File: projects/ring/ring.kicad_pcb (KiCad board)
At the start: 4 copper layers, 10 x 18 mm, 4 parts, among them U1 STM32WB55CEU6TR, Y1 NX1612SA-32.000MHZ-CHP-CIS-3

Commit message: layout and schem changes
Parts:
- removed E1: NN02-101, step-footprints:XCVR_NN02-101
- added C1: C_100nF, Capacitor_SMD:C_0402_1005Metric, F.Cu at (91.0, 39.6)
- added C10: C_100nF, Capacitor_SMD:C_0402_1005Metric, F.Cu at (87.8, 26.6)
- added C11: C_100nF, Capacitor_SMD:C_0402_1005Metric, F.Cu at (90.7, 26.6)
- added C2: C_100nF, Capacitor_SMD:C_0402_1005Metric, F.Cu at (91.0, 41.6)
- added C5: C_100nF, Capacitor_SMD:C_0402_1005Metric, F.Cu at (93.8, 39.6)
- added C6: C_100nF, Capacitor_SMD:C_0402_1005Metric, F.Cu at (93.8, 41.6)
- added C7: C_4.7uF, Capacitor_SMD:C_01005_0402Metric, F.Cu at (96.4, 41.5)
- added C8: C_100nF, Capacitor_SMD:C_0402_1005Metric, F.Cu at (96.7, 39.6)
- added C9: C_4.7uF, Capacitor_SMD:C_01005_0402Metric, F.Cu at (96.4, 43.1)
- added L1: L_10uH_LQM21FN100M70L, Inductor_SMD:L_0805_2012Metric, F.Cu at (87.1, 32.6)
- added L2: L_10nH_LQG15WZ10NJ02D, Inductor_SMD:L_0402_1005Metric, F.Cu at (84.4, 35.5)
- added TP1: Test_Point_SMD, footprints:Test_Point_SMD, F.Cu at (84.0, 39.5)
- added TP2: Test_Point_SMD, footprints:Test_Point_SMD, F.Cu at (84.0, 43.5)
- added TP3: Test_Point_SMD, footprints:Test_Point_SMD, F.Cu at (89.5, 39.5)
- added TP4: Test_Point_SMD, footprints:Test_Point_SMD, F.Cu at (89.5, 43.5)
- added TP5: Test_Point_SMD, footprints:Test_Point_SMD, F.Cu at (95.0, 39.5)
- added U2: LSM6DSO32TR, step-footprints:LSM6DSO32TR, F.Cu at (75.6, 35.8)
- added U3: ANT016008LCS2442MA2, step-footprints:ANT016008LCS2442MA2, F.Cu at (69.8, 20.4)
- added U4: BQ297xy, Package_SON:WSON-6_1.5x1.5mm_P0.5mm, F.Cu at (93.9, 43.0)
- moved Y1 10.2 mm to (78.5, 30.9), turned to 0 degrees
- moved AE1 4.03 mm to (72.2, 23.8)
- moved U1 4.03 mm to (73.2, 29.1)
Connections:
- U1 pad 1: Net-(U1-Pad1) -> Net-(C1-Pad1)
- U1 pad 13: Net-(U1-Pad13) -> /CS
- U1 pad 14: Net-(U1-Pad14) -> /SCK
- U1 pad 15: Net-(U1-Pad15) -> /MISO
- U1 pad 16: Net-(U1-Pad16) -> /MOSI
- U1 pad 20: Net-(U1-Pad20) -> Net-(C1-Pad1)
- U1 pad 22: Net-(U1-Pad22) -> GND
- U1 pad 28: Net-(U1-Pad28) -> /LSM_INT1
- U1 pad 29: Net-(U1-Pad29) -> /LSM_INT2
- U1 pad 32: Net-(U1-Pad32) -> GND
- U1 pad 35: Net-(U1-Pad20) -> Net-(C1-Pad1)
- U1 pad 39: Net-(U1-Pad39) -> /SWDIO
- U1 pad 4: Net-(U1-Pad4) -> /BOOT0
- U1 pad 40: Net-(U1-Pad40) -> Net-(C1-Pad1)
- U1 pad 41: Net-(U1-Pad41) -> /SWCLK
- U1 pad 48: Net-(U1-Pad20) -> Net-(C1-Pad1)
- U1 pad 49: Net-(U1-Pad49) -> GND
- U1 pad 8: Net-(U1-Pad8) -> Net-(C1-Pad1)
- Y1 pad 1: Net-(U1-Pad25) -> Net-(U1-Pad2)
- Y1 pad 3: Net-(U1-Pad24) -> Net-(U1-Pad3)
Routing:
- net Net-(AE1-Pad1): track 1.71 -> 1.06 mm
- added copper zone on F.Cu, net /rad_plane
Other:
- outline, holes or cut-outs redrawn
- board text removed: "10mm Metal Keepout"
- board text removed: "5mm gnd plane"

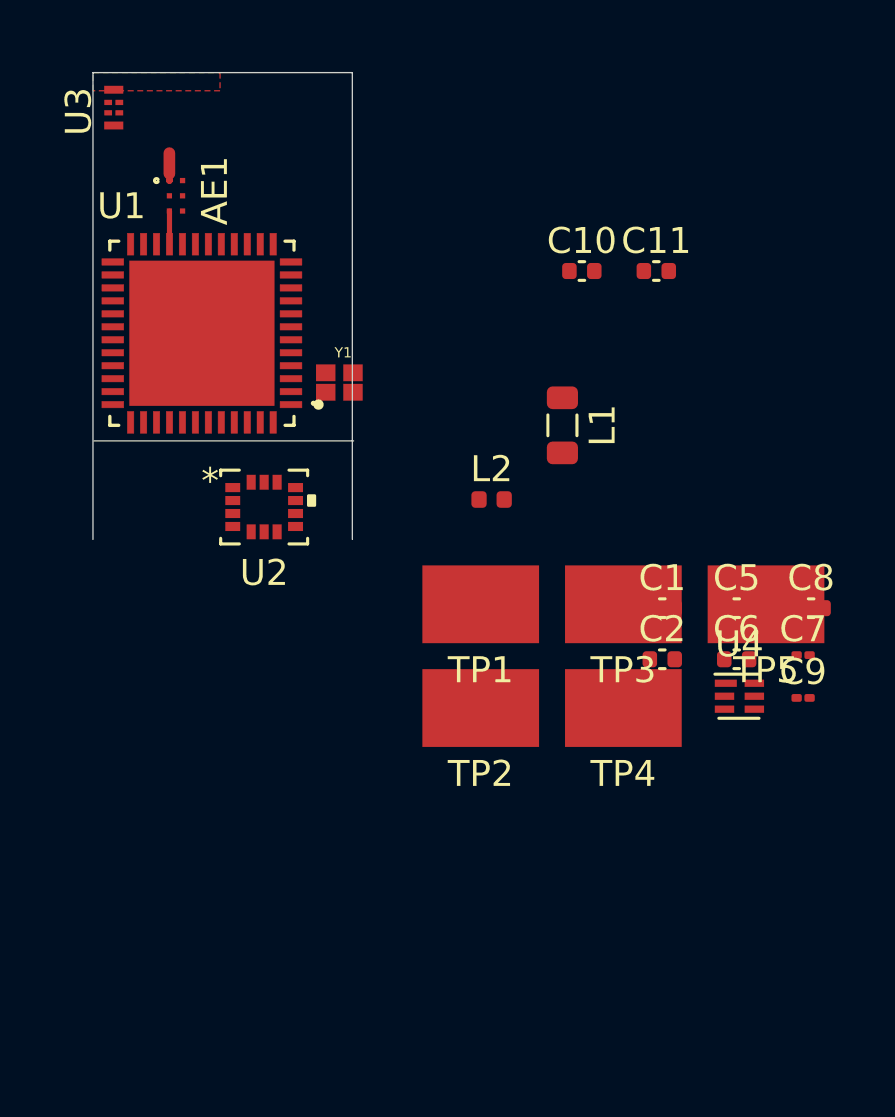
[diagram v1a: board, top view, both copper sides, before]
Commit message: ring hardware schem & layout updates
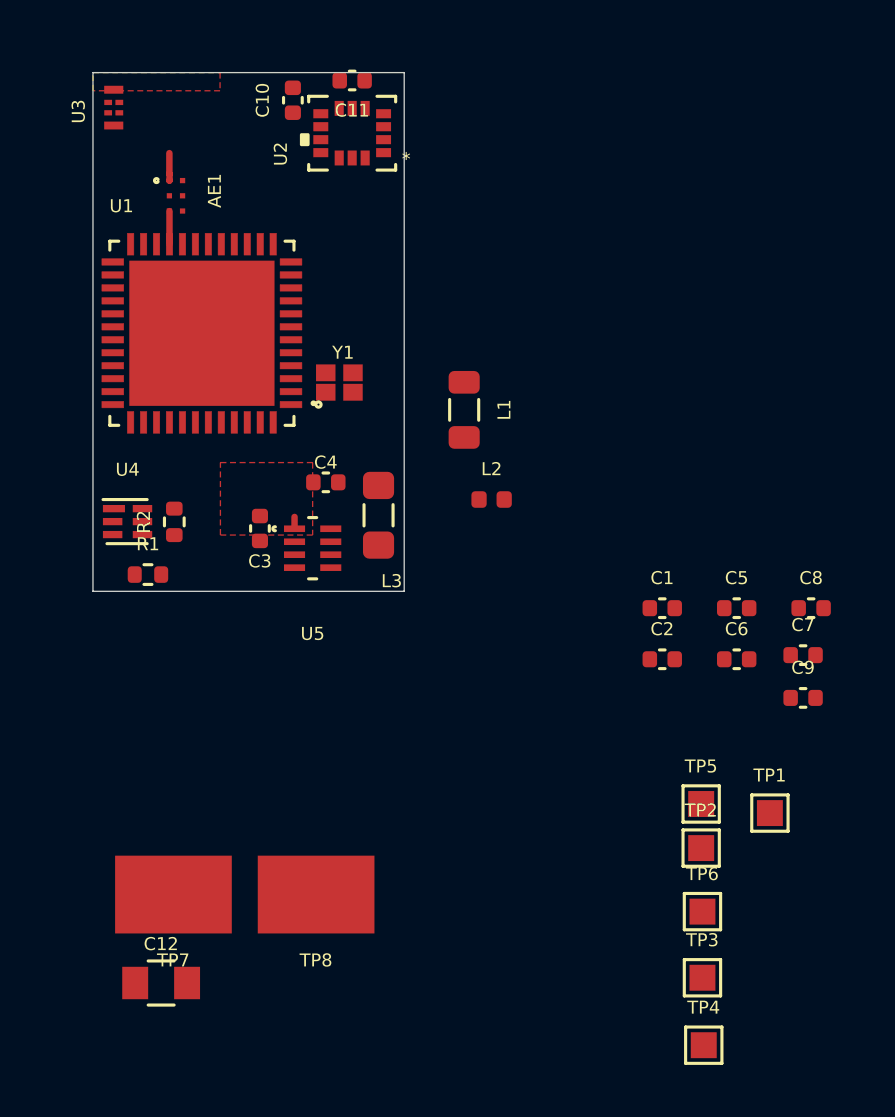
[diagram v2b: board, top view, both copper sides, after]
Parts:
- added C12: C_0.1uF, footprints:C_0805_OEM, F.Cu at (71.6, 54.1)
- added C3: C_4.7uF, Capacitor_SMD:C_0402_1005Metric, F.Cu at (75.4, 36.6)
- added C4: C_10uF, Capacitor_SMD:C_0402_1005Metric, F.Cu at (78.0, 34.8)
- added L3: L_2.2uH, Inductor_SMD:L_0805_2012Metric_Pad1.05x1.20mm_HandSolder, F.Cu at (80.0, 36.1)
- added R1: R_330, Resistor_SMD:R_0402_1005Metric, F.Cu at (71.1, 38.4)
- added R2: R_2.2K, Resistor_SMD:R_0402_1005Metric, F.Cu at (72.1, 36.3)
- added TP6: Test_Point_SMD, TestPoint:TestPoint_Pad_1.0x1.0mm, F.Cu at (92.5, 51.4)
- added TP7: Test_Point_SMD, footprints:Test_Point_SMD, F.Cu at (72.1, 50.7)
- added TP8: Test_Point_SMD, footprints:Test_Point_SMD, F.Cu at (77.6, 50.7)
- added U5: TPS62840DLCR, step-footprints:TPS62840DLCR, F.Cu at (77.5, 37.3)
- C7, C9: footprint Capacitor_SMD:C_01005_0402Metric -> Capacitor_SMD:C_0402_1005Metric
- TP1, TP2, TP3, TP4, TP5: footprint footprints:Test_Point_SMD -> TestPoint:TestPoint_Pad_1.0x1.0mm
- moved U4 24.5 mm to (70.3, 36.3)
- moved U2 14.8 mm to (79.0, 21.3), turned to 180 degrees
- moved TP3 14.7 mm to (92.5, 53.9)
- moved C11 13.8 mm to (79.0, 19.3), turned to 180 degrees
- moved TP1 13.8 mm to (95.1, 47.5)
- moved TP4 13.4 mm to (92.5, 56.5)
- moved C10 12.9 mm to (76.7, 20.1), turned to 90 degrees
- moved TP2 10.1 mm to (92.5, 48.9)
- moved TP5 8.10 mm to (92.5, 47.2)
- moved L1 3.83 mm to (83.3, 32.0)
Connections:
- C1 pad 1: Net-(C1-Pad1) -> +1V8
- C11 pad 1: +BATT -> +1V8
- C2 pad 1: Net-(C1-Pad1) -> +1V8
- C5 pad 1: Net-(C1-Pad1) -> +1V8
- C6 pad 1: Net-(C1-Pad1) -> +1V8
- TP4 pad 1: Net-(TP4-Pad1) -> +BATT
- U1 pad 1: Net-(C1-Pad1) -> +1V8
- U1 pad 20: Net-(C1-Pad1) -> +1V8
- U1 pad 35: Net-(C1-Pad1) -> +1V8
- U1 pad 40: Net-(C1-Pad1) -> +1V8
- U1 pad 48: Net-(C1-Pad1) -> +1V8
- U1 pad 8: Net-(C1-Pad1) -> +1V8
- U2 pad 5: +BATT -> +1V8
- U4 pad 4: Net-(U4-Pad4) -> /CELL-
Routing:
- added copper zone on F.Cu, net GND
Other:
- board size 10 x 18 mm -> 12 x 20 mm
- rule via_min_drill: 0.3 -> 0.2

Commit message: nearly complete first pass schem, RF ready for review
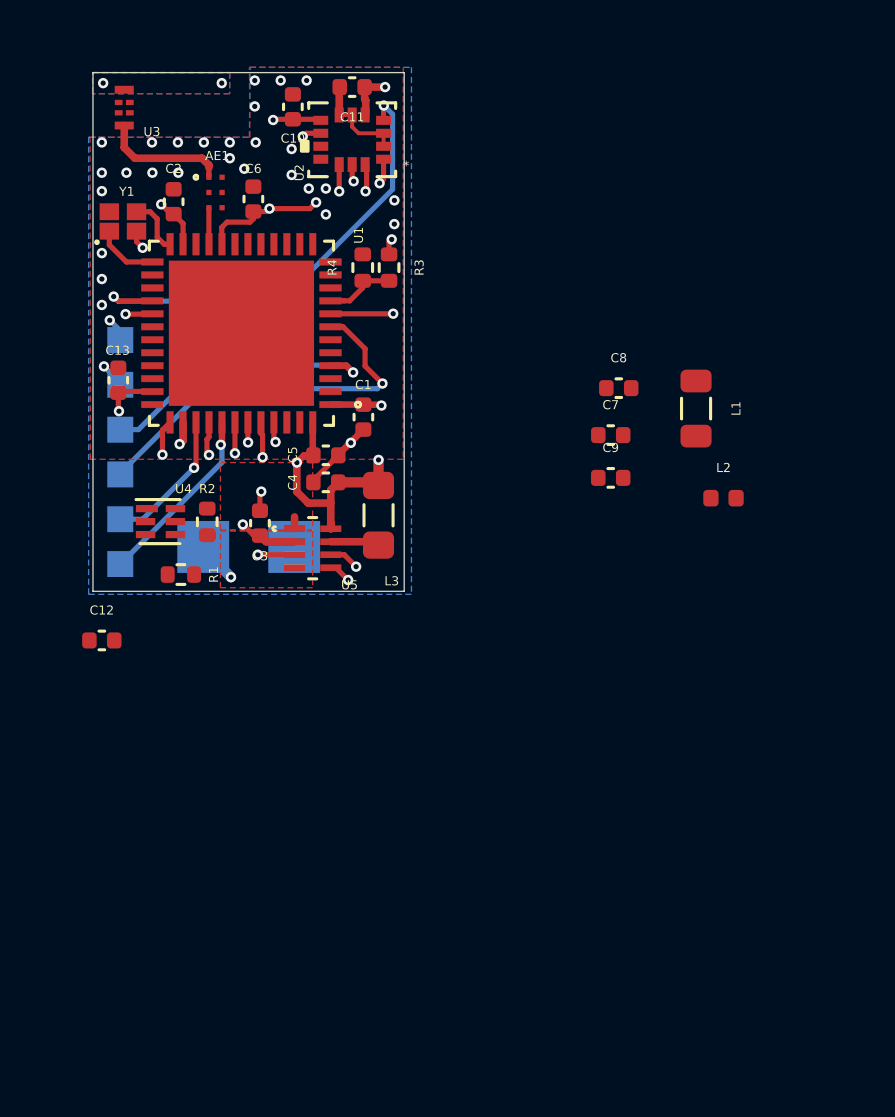
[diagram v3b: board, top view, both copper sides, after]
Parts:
- added C13: C_100nF, Capacitor_SMD:C_0402_1005Metric, F.Cu at (70.0, 30.9)
- added R3: R_200K, Resistor_SMD:R_0402_1005Metric, F.Cu at (80.4, 26.5)
- added R4: R_100K, Resistor_SMD:R_0402_1005Metric, F.Cu at (79.4, 26.5)
- C12: footprint footprints:C_0805_OEM -> Capacitor_SMD:C_0402_1005Metric
- TP1, TP2, TP3, TP4, TP5, TP6: moved to B.Cu
- TP7, TP8: footprint footprints:Test_Point_SMD -> TestPoint:TestPoint_Pad_2.0x2.0mm; moved to B.Cu
- moved TP4 31.5 mm to (70.1, 34.5)
- moved TP6 31.5 mm to (70.1, 29.3)
- moved TP3 30.8 mm to (70.1, 32.8)
- moved TP5 27.6 mm to (70.1, 31.0)
- moved TP1 27.5 mm to (70.1, 36.2)
- moved C2 25.8 mm to (72.1, 24.0), turned to 90 degrees
- moved C6 25.7 mm to (75.2, 23.9), turned to 90 degrees
- moved TP2 24.9 mm to (70.1, 37.9)
- moved C5 16.9 mm to (78.0, 33.8)
- moved C1 13.7 mm to (79.4, 32.3), turned to 270 degrees
- moved TP7 13.5 mm to (73.3, 37.3)
- moved TP8 13.4 mm to (76.8, 37.3)
- moved C12 13.4 mm to (69.3, 40.9)
- moved C7 11.3 mm to (89.0, 33.0)
- moved C9 11.3 mm to (89.0, 34.6)
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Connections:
- net /rad_plane renamed /RAD_PLANE
- net Net-(U4-Pad2) renamed /C_gate
- net Net-(U4-Pad3) renamed /D_gate
- C10 pad 1: +BATT -> +1V8
- TP4 pad 1: +BATT -> /NRST
- U1 pad 13: /CS -> Net-(U1-Pad13)
- U1 pad 14: /SCK -> Net-(U1-Pad14)
- U1 pad 15: /MISO -> Net-(U1-Pad15)
- U1 pad 16: /MOSI -> Net-(U1-Pad16)
- U1 pad 23: Net-(U1-Pad23) -> +1V8
- U1 pad 37: Net-(U1-Pad37) -> /TPS_MODE
- U1 pad 38: Net-(U1-Pad38) -> /TPS_STOP
- U1 pad 42: Net-(U1-Pad42) -> /CS
- U1 pad 43: Net-(U1-Pad43) -> /SCK
- U1 pad 44: Net-(U1-Pad44) -> /MISO
- U1 pad 45: Net-(U1-Pad45) -> /MOSI
- U1 pad 7: Net-(U1-Pad7) -> /NRST
- U1 pad 9: Net-(U1-Pad9) -> /BATT_LVL
- U2 pad 8: +BATT -> +1V8
- Y1 pad 1: Net-(U1-Pad2) -> Net-(U1-Pad25)
- Y1 pad 3: Net-(U1-Pad3) -> Net-(U1-Pad24)
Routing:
- net +1V8: track 0.00 -> 29.9 mm, vias 0 -> 12
- net /LSM_INT1: track 0.00 -> 18.1 mm, vias 0 -> 2
- net /MISO: track 0.00 -> 15.4 mm, vias 0 -> 2
- net /NRST: track 0.00 -> 14.9 mm, vias 0 -> 1
- net /LSM_INT2: track 0.00 -> 14.8 mm, vias 0 -> 2
- net /CS: track 0.00 -> 14.0 mm, vias 0 -> 2
- net /SCK: track 0.00 -> 13.2 mm, vias 0 -> 2
- net /MOSI: track 0.00 -> 13.0 mm, vias 0 -> 2
- net +BATT: track 0.00 -> 12.0 mm, vias 0 -> 3
- net /TPS_STOP: track 0.00 -> 11.8 mm, vias 0 -> 2
- net /BOOT0: track 0.00 -> 11.1 mm, vias 0 -> 1
- net GND: track 0.46 -> 10.9 mm, vias 0 -> 32
- net /TPS_MODE: track 0.00 -> 8.85 mm, vias 0 -> 2
- net /SWCLK: track 0.00 -> 7.13 mm, vias 0 -> 1
- net /SWDIO: track 0.00 -> 5.45 mm, vias 0 -> 1
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- added copper zone on In2.Cu, net +1V8
- added copper zone on F.Cu, net +BATT
- added copper zone on B.Cu, net /rad_plane
- added copper zone on In1.Cu, net /rad_plane
- added copper zone on In2.Cu, net /rad_plane
- added copper zone on B.Cu, net GND
- added copper zone on In1.Cu, net GND
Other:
- rule trace_min: 0.2 -> 0.15

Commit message: an inch closer to hardware first rev completion
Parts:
- removed C7, C9: C_4.7uF, Capacitor_SMD:C_0402_1005Metric
- removed C8: C_100nF, Capacitor_SMD:C_0402_1005Metric
- removed L1: L_10uH_LQM21FN100M70L, Inductor_SMD:L_0805_2012Metric
- removed L2: L_10nH_LQG15WZ10NJ02D, Inductor_SMD:L_0402_1005Metric
- added D1: LED_Amber, LED_SMD:LED_0402_1005Metric, B.Cu at (79.4, 28.7)
- added Q1: CSD17318Q2T, step-footprints:TRANS_CSD17318Q2T, F.Cu at (72.7, 37.5)
- added Q2: CSD17318Q2T, step-footprints:TRANS_CSD17318Q2T, F.Cu at (70.6, 37.5)
- added R5: R_1K, Resistor_SMD:R_0402_1005Metric, B.Cu at (78.4, 28.7)
- added TP10: Test_Point_SMD, TestPoint:TestPoint_Pad_1.0x1.0mm, B.Cu at (76.0, 27.9)
- added TP11: Test_Point_SMD, TestPoint:TestPoint_Pad_1.0x1.0mm, B.Cu at (73.6, 29.5)
- added TP12: Test_Point_SMD, TestPoint:TestPoint_Pad_1.0x1.0mm, B.Cu at (73.6, 27.9)
- added TP13: Test_Point_SMD, TestPoint:TestPoint_Pad_1.0x1.0mm, B.Cu at (79.0, 25.4)
- added TP9: Test_Point_SMD, TestPoint:TestPoint_Pad_1.0x1.0mm, B.Cu at (76.0, 29.5)
- TP7, TP8: footprint TestPoint:TestPoint_Pad_2.0x2.0mm -> TestPoint:TestPoint_Pad_1.5x1.5mm
- moved C12 8.50 mm to (76.0, 35.6), turned to 180 degrees
- moved R1 5.21 mm to (76.0, 34.6)
- moved R2 2.59 mm to (71.5, 34.5), turned to 0 degrees
- moved U4 2.47 mm to (73.8, 35.1)
- moved C3 1.20 mm to (74.9, 37.4), turned to 270 degrees
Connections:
- U1 pad 13: Net-(U1-Pad13) -> /BTN_0
- U1 pad 14: Net-(U1-Pad14) -> /BTN_1
- U1 pad 15: Net-(U1-Pad15) -> /BTN_2
- U1 pad 16: Net-(U1-Pad16) -> /BTN_3
- U1 pad 31: Net-(U1-Pad31) -> +1V8
- U1 pad 33: Net-(U1-Pad33) -> +1V8
- U1 pad 34: Net-(U1-Pad34) -> +1V8
- U1 pad 6: Net-(U1-Pad6) -> /LED_1
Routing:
- net /LSM_INT1: track 18.1 -> 8.20 mm
- net +BATT: track 12.0 -> 3.98 mm, vias 3 -> 2
- net /BTN_2: track 0.00 -> 7.01 mm, vias 0 -> 1
- net /BTN_0: track 0.00 -> 6.60 mm, vias 0 -> 1
- net /CELL-: track 0.00 -> 6.14 mm, vias 0 -> 1
- net /LSM_INT2: track 14.8 -> 9.33 mm
- net /D_gate: track 0.00 -> 5.07 mm, vias 0 -> 1
- net /BTN_3: track 0.00 -> 4.96 mm, vias 0 -> 1
- net /BTN_1: track 0.00 -> 4.79 mm, vias 0 -> 1
- net /C_gate: track 0.00 -> 3.98 mm
- net Net-(C12-Pad1): track 0.00 -> 2.79 mm
- net /LED_1: track 0.00 -> 2.61 mm, vias 0 -> 1
- net /NRST: track 14.9 -> 17.2 mm
- net Net-(D1-Pad1): track 0.00 -> 1.03 mm
- net +1V8: track 29.9 -> 30.6 mm
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- added copper zone on F.Cu, net /DRAIN
- added copper zone on B.Cu, net /RAD_PLANE
- added copper zone on In1.Cu, net /RAD_PLANE
- added copper zone on In2.Cu, net /RAD_PLANE
- removed copper zone on B.Cu, net /rad_plane
- removed copper zone on In1.Cu, net /rad_plane
- removed copper zone on In2.Cu, net /rad_plane
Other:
- board text added: "+"
- board text added: "-"
- board text added: "1V8"
- board text added: "BOOT0"
- board text added: "GND"
- board text added: "NRST"
- board text added: "SWCLK"
- board text added: "SWDIO"

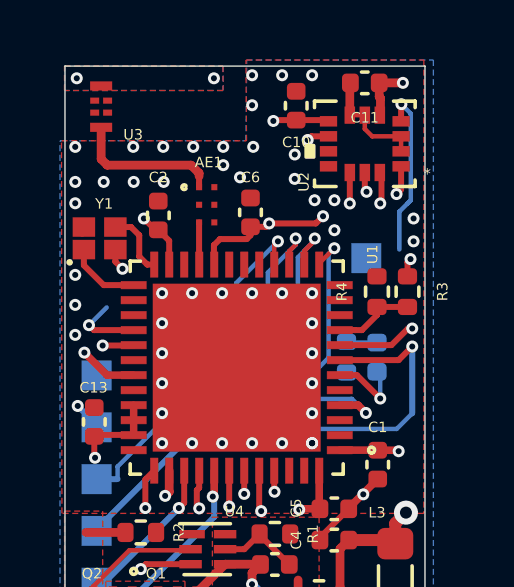
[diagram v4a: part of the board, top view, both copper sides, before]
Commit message: AOCA NMOS package update
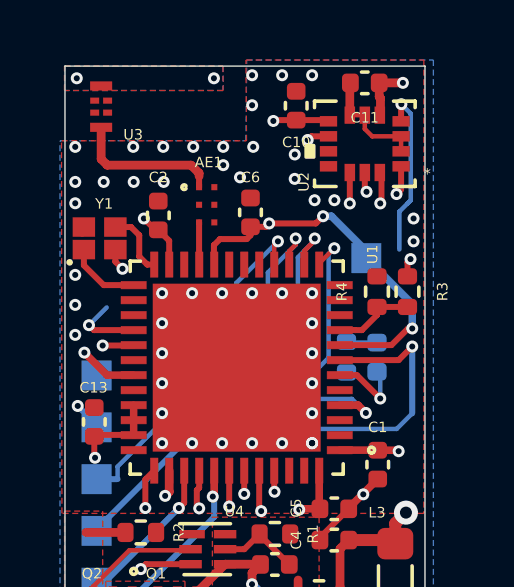
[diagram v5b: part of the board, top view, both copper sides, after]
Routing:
- net +1V8: track 30.6 -> 35.8 mm
- net GND: vias 52 -> 51

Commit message: int2, silkscreen, DRC DRC DRC FUCK
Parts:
- removed Q2: CSD17318Q2T, step-footprints:TRANS_CSD17318Q2T
- Q1: value CSD17318Q2T -> AOCA32116E; footprint step-footprints:TRANS_CSD17318Q2T -> step-footprints:AOCA32116E
- moved C12 2.39 mm to (73.8, 36.4), turned to 270 degrees
- moved Q1 2.16 mm to (70.7, 38.1)
- moved U4 2.12 mm to (72.0, 36.3)
- moved R1 1.80 mm to (74.2, 35.0)
- moved C3 0.81 mm to (74.3, 38.0), turned to 180 degrees
- moved R2 0.43 mm to (71.9, 34.7)
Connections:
- Q1 pad 1: /DRAIN -> /CELL-
- Q1 pad 2: /DRAIN -> GND
- Q1 pad 3: /D_gate -> /C_gate
- Q1 pad 4: /CELL- -> /D_gate
- TP7 pad 1: +BATT -> /CELL-
- TP8 pad 1: /CELL- -> +BATT
- U1 pad 12: Net-(U1-Pad12) -> /LSM_INT1
- U1 pad 28: /LSM_INT1 -> Net-(U1-Pad28)
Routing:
- net +BATT: track 3.98 -> 21.9 mm, vias 2 -> 5
- net GND: track 11.4 -> 15.2 mm, vias 51 -> 47
- net /D_gate: track 5.07 -> 1.58 mm, vias 1 -> 0
- net /C_gate: track 3.98 -> 2.44 mm
- net Net-(R2-Pad2): track 0.00 -> 1.16 mm
- net /TPS_MODE: track 8.85 -> 9.50 mm
- removed copper zone on F.Cu, net /DRAIN

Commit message: ready for first review
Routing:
- net /LSM_INT2: track 9.33 -> 14.9 mm
- net +1V8: track 35.8 -> 37.1 mm
- net /BTN_0: track 6.60 -> 5.97 mm
- net +BATT: track 21.9 -> 22.5 mm
- net GND: track 15.2 -> 15.1 mm, vias 47 -> 45
- net (no net): vias 0 -> 1
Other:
- board text added: ">ALPDSA<"
- board text added: "B0"
- board text added: "B1"
- board text added: "B2"
- board text added: "B3"
- board text added: "BOOT"
- board text added: "CLK"
- board text added: "DIO"
- board text added: "DNP"
- board text added: "F*** ORII"
- board text added: "RING V0.0"
- board text added: "RST"
- board text added: "[STEP AFTERHOURS]"
- board text added: "~NEON RAINBOWS~"
- board text added: "~PCB POLICE~ ~WAS HERE~"
- board text removed: "BOOT0"
- board text removed: "NRST"
- board text removed: "SWCLK"
- board text removed: "SWDIO"

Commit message: ready for first pass fr this time fixed 'spelling':
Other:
- board text added: "F ORII"
- board text removed: "F*** ORII"
